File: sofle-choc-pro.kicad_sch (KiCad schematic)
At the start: 194 parts, among them J1 Connector, USB-TYPE-C-16P, J2 Connector, USB-TYPE-C-16P, J3 OLED 128x32, SW1 BOOT, SW10 F0, SW11 F1, SW12 F2, SW13 F3, SW14 F4, SW15 F5, SW16 F6 Choc/EC11, SW2 RESET, SW20 N0, SW21 N1, SW22 N2, SW23 N3, SW24 N4, SW25 N5, SW30 T0, SW31 T1, SW32 T2, SW33 T3, SW34 T4, SW35 T5, SW40 H0, SW41 H1, SW42 H2, SW43 H3, SW44 H4, SW45 H5, SW50 B0, SW51 B1, SW52 B2, SW53 B3, SW54 B4, SW55 B5, SW60 TH0, SW61 TH1, SW62 TH2, SW63 TH3, SW64 TH4, SW65 TH5 Choc/EC11, U1 RP2040, U2 USBLC6-2P6, U3 W25Q128JVPIQ, U4 USBLC6-2P6, U5 AP2112K-3.3, U6 SN74LV1T34DBVR, X1 ABM8-272-T3

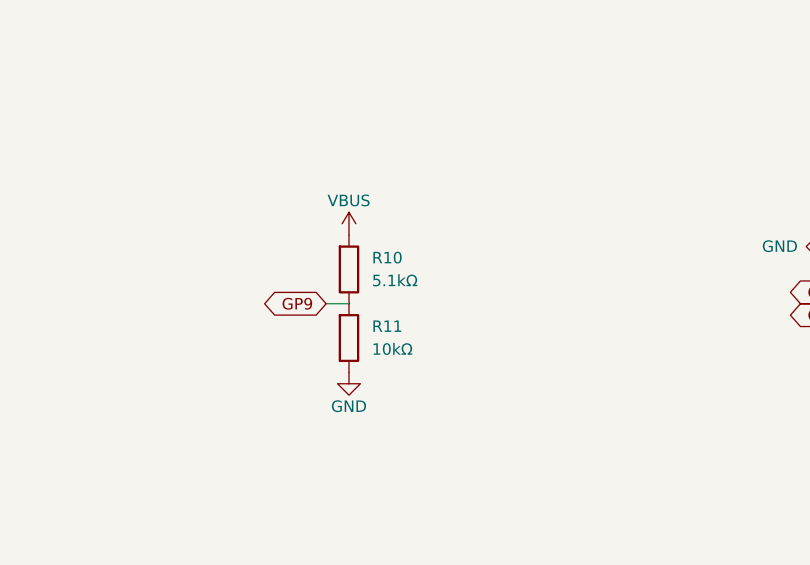
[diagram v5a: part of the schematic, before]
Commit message: fix(pcb): prepare the left half for jlcpcb assembly
Fixes the VBUS sense divider and sets every fabrication field the
Fabrication Toolkit plugin needs, then commits its JLCPCB outputs.

- R10 is now 10k like R11: GP9 sees 2.2 to 2.75 V over 4.4 to 5.5 V
  VBUS, inside the RP2040's 2.0 V to IOVDD + 0.3 V input window (the
  old 5.1k gave 3.64 V at 5.5 V)
- FT Rotation Offset 270 on U2, U3, U4 and 180 on U6, found by fitting
  JLC's own footprints onto ours
- FT Position Offset 0,1.394 on J1/J2, measured through the locating
  pegs of JLC's C165948 footprint
- Hotswap sockets, J3 and JP1 leave the position file; the 72 socket
  pads lose their paste on the board and in the library footprints
- U2/U4 fields named a stale SRV05-4 part; now USBLC6-2P6 (LCSC was
  already right)
- production/: Gerbers, BOM, CPL and IPC netlist from the plugin, run
  without auto-translate (it would wrongly rotate U5)

ERC 0, DRC 0 with schematic parity. CPL positions match JLC's
footprint origins within 0.03 mm.
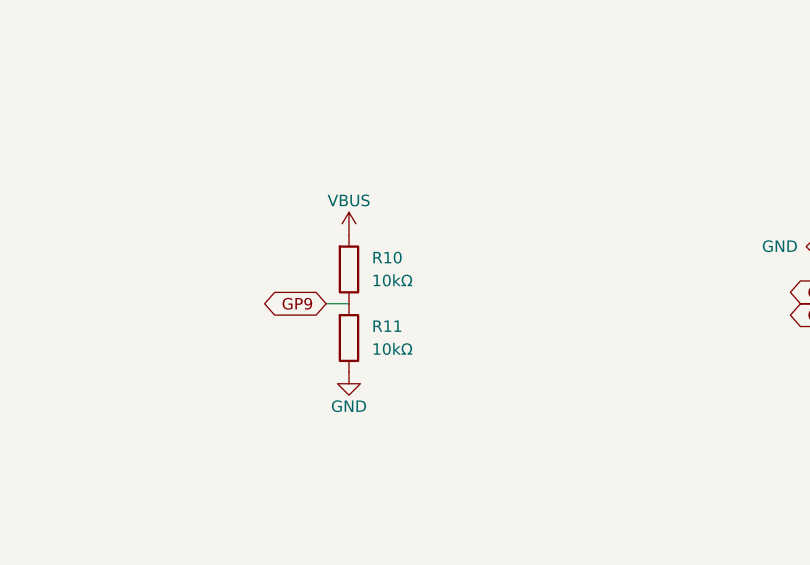
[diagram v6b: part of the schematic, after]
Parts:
- J1, J2: FT Position Offset (none) -> 0,1.394
- R10: value 5.1kΩ -> 10kΩ; symbol PCM_JLCPCB-Resistors:0402,5.1kΩ -> PCM_JLCPCB-Resistors:0402,10kΩ; LCSC C25905 -> C25744; Part 0402WGF5101TCE -> 0402WGF1002TCE; Resistance 5.1kΩ -> 10kΩ
- U2, U4: Class Preferred Component -> Extended Component; FT Rotation Offset (none) -> 270; Manufacturer MSKSEMI -> R+O; Part SRV05-4 -> USBLC6-2P6
- U3: FT Rotation Offset (none) -> 270
- U6: FT Rotation Offset (none) -> 180
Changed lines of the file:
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@@
 			)
 		)
+		(property "FT Position Offset" "0,1.394"
+			(at 29.21 39.37 0)
+			(hide yes)
+			(show_name no)
+			(do_not_autoplace no)
+			(effects
+				(font
+					(size 1.27 1.27)
+				)
+			)
+		)
 		(pin "B8"
 		)
@@
 		(in_bom no)
 		(on_board yes)
-		(in_pos_files yes)
+		(in_pos_files no)
 		(dnp no)
 		(property "Reference" "SW54"
@@
 		(in_bom no)
 		(on_board yes)
-		(in_pos_files yes)
+		(in_pos_files no)
 		(dnp no)
 		(property "Reference" "SW16"
@@
 		(in_bom no)
 		(on_board yes)
-		(in_pos_files yes)
+		(in_pos_files no)
 		(dnp no)
 		(property "Reference" "SW35"
@@
 		(in_bom no)
 		(on_board yes)
-		(in_pos_files yes)
+		(in_pos_files no)
 		(dnp no)
 		(property "Reference" "SW20"
@@
 		(in_bom no)
 		(on_board yes)
-		(in_pos_files yes)
+		(in_pos_files no)
 		(dnp no)
 		(property "Reference" "SW65"
@@
 		(in_bom no)
 		(on_board yes)
-		(in_pos_files yes)
+		(in_pos_files no)
 		(dnp no)
 		(property "Reference" "SW12"
@@
 		(in_bom no)
 		(on_board yes)
-		(in_pos_files yes)
+		(in_pos_files no)
 		(dnp no)
 		(property "Reference" "SW63"
@@
 		(in_bom no)
 		(on_board yes)
-		(in_pos_files yes)
+		(in_pos_files no)
 		(dnp no)
 		(property "Reference" "SW24"
@@
 		(in_bom no)
 		(on_board yes)
-		(in_pos_files yes)
+		(in_pos_files no)
 		(dnp no)
 		(property "Reference" "SW10"
@@
 			)
 		)
+		(property "FT Position Offset" "0,1.394"
+			(at 109.22 271.78 0)
+			(hide yes)
+			(show_name no)
+			(do_not_autoplace no)
+			(effects
+				(font
+					(size 1.27 1.27)
+				)
+			)
+		)
 		(pin "A12B1"
 		)
@@
 		(in_bom no)
 		(on_board yes)
-		(in_pos_files yes)
+		(in_pos_files no)
 		(dnp no)
 		(property "Reference" "SW25"
@@
 		(in_bom no)
 		(on_board yes)
-		(in_pos_files yes)
+		(in_pos_files no)
 		(dnp no)
 		(property "Reference" "SW52"
@@
 			)
 		)
-		(property "Description" "4A 15V 80W 6V Unidirectional 5V SOT-23-6 ESD and Surge Protection (TVS/ESD) ROHS"
+		(property "Description" "USB ESD protection, 2 data lines and VBUS, SOT-563"
 			(at 50.8 217.17 0)
 			(hide yes)
@@
 			)
 		)
+		(property "FT Rotation Offset" "270"
+			(at 50.8 217.17 0)
+			(hide yes)
+			(show_name no)
+			(do_not_autoplace no)
+			(effects
+				(font
+					(size 1.27 1.27)
+				)
+			)
+		)
 		(property "Stock" ""
 			(at 50.8 217.17 0)
@@
 			)
 		)
-		(property "Class" "Preferred Component"
+		(property "Class" "Extended Component"
 			(at 50.8 217.17 0)
 			(hide yes)
@@
 			)
 		)
-		(property "Manufacturer" "MSKSEMI"
+		(property "Manufacturer" "R+O"
 			(at 50.8 217.17 0)
 			(hide yes)
@@
 			)
 		)
-		(property "Part" "SRV05-4"
+		(property "Part" "USBLC6-2P6"
 			(at 50.8 217.17 0)
 			(hide yes)
@@
 		(in_bom no)
 		(on_board yes)
-		(in_pos_files yes)
+		(in_pos_files no)
 		(dnp no)
 		(property "Reference" "SW33"
@@
 		(in_bom no)
 		(on_board yes)
-		(in_pos_files yes)
+		(in_pos_files no)
 		(dnp no)
 		(property "Reference" "SW40"
@@
 		(in_bom no)
 		(on_board yes)
-		(in_pos_files yes)
+		(in_pos_files no)
 		(dnp no)
 		(property "Reference" "SW61"
@@
 		(in_bom no)
 		(on_board yes)
-		(in_pos_files yes)
+		(in_pos_files no)
 		(dnp no)
 		(property "Reference" "SW64"
@@
 		(in_bom no)
 		(on_board yes)
-		(in_pos_files yes)
+		(in_pos_files no)
 		(dnp no)
 		(property "Reference" "SW45"
@@
 		(in_bom no)
 		(on_board yes)
-		(in_pos_files yes)
+		(in_pos_files no)
 		(dnp no)
 		(property "Reference" "SW50"
@@
 			)
 		)
+		(property "FT Rotation Offset" "180"
+			(at 299.72 91.44 0)
+			(hide yes)
+			(show_name no)
+			(do_not_autoplace no)
+			(effects
+				(font
+					(size 1.27 1.27)
+				)
+			)
+		)
 		(pin "1"
 		)
@@
 		(in_bom no)
 		(on_board yes)
-		(in_pos_files yes)
+		(in_pos_files no)
 		(dnp no)
 		(property "Reference" "SW15"
@@
 		(in_bom no)
 		(on_board yes)
-		(in_pos_files yes)
+		(in_pos_files no)
 		(dnp no)
 		(property "Reference" "SW43"
@@
 		(in_bom no)
 		(on_board yes)
-		(in_pos_files yes)
+		(in_pos_files no)
 		(dnp no)
 		(property "Reference" "SW44"
@@
 		(in_bom no)
 		(on_board yes)
-		(in_pos_files yes)
+		(in_pos_files no)
 		(dnp no)
 		(property "Reference" "SW32"
@@
 		(in_bom no)
 		(on_board yes)
-		(in_pos_files yes)
+		(in_pos_files no)
 		(dnp no)
 		(property "Reference" "J3"
@@
 		(in_bom no)
 		(on_board yes)
-		(in_pos_files yes)
+		(in_pos_files no)
 		(dnp no)
 		(property "Reference" "SW51"
@@
 		(in_bom no)
 		(on_board yes)
-		(in_pos_files yes)
+		(in_pos_files no)
 		(dnp no)
 		(property "Reference" "SW41"
@@
 		(in_bom no)
 		(on_board yes)
-		(in_pos_files yes)
+		(in_pos_files no)
 		(dnp no)
 		(property "Reference" "SW21"
@@
 		(in_bom no)
 		(on_board yes)
-		(in_pos_files yes)
+		(in_pos_files no)
 		(dnp no)
 		(property "Reference" "SW34"
@@
 		(in_bom no)
 		(on_board yes)
-		(in_pos_files yes)
+		(in_pos_files no)
 		(dnp no)
 		(property "Reference" "SW53"
@@
 		(in_bom no)
 		(on_board yes)
-		(in_pos_files yes)
+		(in_pos_files no)
 		(dnp no)
 		(property "Reference" "SW14"
@@
 		(in_bom no)
 		(on_board yes)
-		(in_pos_files yes)
+		(in_pos_files no)
 		(dnp no)
 		(property "Reference" "SW22"
@@
 		(in_bom no)
 		(on_board yes)
-		(in_pos_files yes)
+		(in_pos_files no)
 		(dnp no)
 		(property "Reference" "SW42"
@@
 		(in_bom no)
 		(on_board yes)
-		(in_pos_files yes)
+		(in_pos_files no)
 		(dnp no)
 		(property "Reference" "SW13"
@@
 		(in_bom no)
 		(on_board yes)
-		(in_pos_files yes)
+		(in_pos_files no)
 		(dnp no)
 		(property "Reference" "JP1"
@@
 			)
 		)
-		(property "Description" "4A 15V 80W 6V Unidirectional 5V SOT-23-6 ESD and Surge Protection (TVS/ESD) ROHS"
+		(property "Description" "USB ESD protection, 2 data lines and VBUS, SOT-563"
 			(at 50.8 266.7 0)
 			(hide yes)
@@
 			)
 		)
+		(property "FT Rotation Offset" "270"
+			(at 50.8 266.7 0)
+			(hide yes)
+			(show_name no)
+			(do_not_autoplace no)
+			(effects
+				(font
+					(size 1.27 1.27)
+				)
+			)
+		)
 		(property "Stock" ""
 			(at 50.8 266.7 0)
@@
 			)
 		)
-		(property "Class" "Preferred Component"
+		(property "Class" "Extended Component"
 			(at 50.8 266.7 0)
 			(hide yes)
@@
 			)
 		)
-		(property "Manufacturer" "MSKSEMI"
+		(property "Manufacturer" "R+O"
 			(at 50.8 266.7 0)
 			(hide yes)
@@
 			)
 		)
-		(property "Part" "SRV05-4"
+		(property "Part" "USBLC6-2P6"
 			(at 50.8 266.7 0)
 			(hide yes)
@@
 		(in_bom no)
 		(on_board yes)
-		(in_pos_files yes)
+		(in_pos_files no)
 		(dnp no)
 		(property "Reference" "SW31"
@@
 	)
 	(symbol
-		(lib_id "PCM_JLCPCB-Resistors:0402,5.1kΩ")
+		(lib_id "PCM_JLCPCB-Resistors:0402,10kΩ")
 		(at 254 40.64 0)
 		(unit 1)
@@
 			)
 		)
-		(property "Value" "5.1kΩ"
+		(property "Value" "10kΩ"
 			(at 256.54 41.91 0)
 			(show_name no)
@@
 			)
 		)
-		(property "Datasheet" "https://www.lcsc.com/datasheet/lcsc_datasheet_2206010045_UNI-ROYAL-Uniroyal-Elec-0402WGF5101TCE_C25905.pdf"
+		(property "Datasheet" "https://www.lcsc.com/datasheet/lcsc_datasheet_2411221126_UNI-ROYAL-Uniroyal-Elec-0402WGF1002TCE_C25744.pdf"
 			(at 254 40.64 0)
 			(hide yes)
@@
 			)
 		)
-		(property "Description" "62.5mW Thick Film Resistors 50V ±100ppm/°C ±1% 5.1kΩ 0402 Chip Resistor - Surface Mount ROHS"
+		(property "Description" "62.5mW Thick Film Resistors 50V ±100ppm/°C ±1% 10kΩ 0402 Chip Resistor - Surface Mount ROHS"
 			(at 254 40.64 0)
 			(hide yes)
@@
 			)
 		)
-		(property "LCSC" "C25905"
+		(property "LCSC" "C25744"
 			(at 254 40.64 0)
 			(hide yes)
@@
 			)
 		)
-		(property "Part" "0402WGF5101TCE"
+		(property "Part" "0402WGF1002TCE"
 			(at 254 40.64 0)
 			(hide yes)
@@
 			)
 		)
-		(property "Resistance" "5.1kΩ"
+		(property "Resistance" "10kΩ"
 			(at 254 40.64 0)
 			(hide yes)
@@
 		(in_bom no)
 		(on_board yes)
-		(in_pos_files yes)
+		(in_pos_files no)
 		(dnp no)
 		(property "Reference" "SW23"
@@
 		(in_bom no)
 		(on_board yes)
-		(in_pos_files yes)
+		(in_pos_files no)
 		(dnp no)
 		(property "Reference" "SW11"
@@
 		(in_bom no)
 		(on_board yes)
-		(in_pos_files yes)
+		(in_pos_files no)
 		(dnp no)
 		(property "Reference" "SW55"
@@
 		(in_bom no)
 		(on_board yes)
-		(in_pos_files yes)
+		(in_pos_files no)
 		(dnp no)
 		(property "Reference" "SW62"
@@
 		(in_bom no)
 		(on_board yes)
-		(in_pos_files yes)
+		(in_pos_files no)
 		(dnp no)
 		(property "Reference" "SW60"
@@
 		(in_bom no)
 		(on_board yes)
-		(in_pos_files yes)
+		(in_pos_files no)
 		(dnp no)
 		(property "Reference" "SW30"
@@
 			(at 55.88 171.45 0)
 			(hide yes)
+			(show_name no)
+			(do_not_autoplace no)
+			(effects
+				(font
+					(size 1.27 1.27)
+				)
+			)
+		)
+		(property "FT Rotation Offset" "270"
+			(at 55.88 171.45 0)
+			(hide yes)
